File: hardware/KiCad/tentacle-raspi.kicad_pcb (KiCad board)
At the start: 2 copper layers, 65 x 56.5 mm, 37 parts, among them P101 CONN_01X06, P102 CONN_01X06, P201 BNC, P301 BNC, P401 BNC

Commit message: Version 2.0
1wire sensor
flow sensor
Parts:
- removed P102: CONN_01X06, temp_terminal:WL-PINH_1X6_snk
- removed P401: BNC, temp_terminal:WL-EB08040502_snk
- removed STP401: EZO_SMD, temp_terminal:WL-ezo-smd
- added J1: Conn_01x03, Connector_Phoenix_MC:PhoenixContact_MC_1,5_3-G-3.5_1x03_P3.50mm_Horizontal, F.Cu at (153.5, 105.3)
- added J2: Conn_01x03, Connector_Phoenix_MC:PhoenixContact_MC_1,5_3-G-3.5_1x03_P3.50mm_Horizontal, F.Cu at (162.2, 98.0)
- added R1: 4.7K, temp_terminal:WL-SM0805R, F.Cu at (157.7, 95.5)
- added R2: 4.7K, temp_terminal:WL-SM0805R, F.Cu at (156.0, 99.8)
- moved R101 6.25 mm to (162.6, 75.4)
- moved R102 3.97 mm to (162.6, 79.9), turned to -90 degrees
- moved fiducial 1.86 mm to (165.4, 106.2)
- moved fiducial 1.78 mm to (109.2, 65.3)
- moved fiducial 0.57 mm to (107.4, 65.3)
- moved PI_Board 0.55 mm to (138.0, 61.5)
- moved P101 0.21 mm to (167.6, 72.6)
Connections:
- PI_BOARD101 pad 33: unconnected-(PI_BOARD101-Pad33) -> /nonisolated1/TEMP
- PI_BOARD101 pad 37: unconnected-(PI_BOARD101-Pad37) -> /nonisolated1/FLOW
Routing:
- net +3.3V: track 144.6 -> 66.5 mm, vias 3 -> 2
- net /SDA: track 162.9 -> 99.0 mm, vias 5 -> 4
- net /nonisolated1/TEMP: track 0.00 -> 44.0 mm
- net /nonisolated1/FLOW: track 0.00 -> 36.5 mm
- net /SCL: track 135.3 -> 104.6 mm, vias 5 -> 4
- net Net-(R302-Pad2): track 42.9 -> 33.0 mm
- net GND: track 56.5 -> 49.4 mm, vias 13 -> 12
- net Net-(P401-Pad1): track 6.56 -> 0.00 mm
- net Net-(P401-Pad2): track 6.43 -> 0.00 mm
- net Net-(P102-Pad5): track 2.57 -> 0.00 mm
- added copper zone on F.Cu, net +3.3V
- removed copper zone on F.Cu, net GND
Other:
- board text added: "FLOW"
- board text added: "I2C AUX CHANNEL"
- board text added: "TEMP"
- board text removed: "CHANNEL 3"
- board text removed: "CHANNEL 4"
- board text removed: "CHANNEL 5"
- board text removed: "NON ISOLATED"

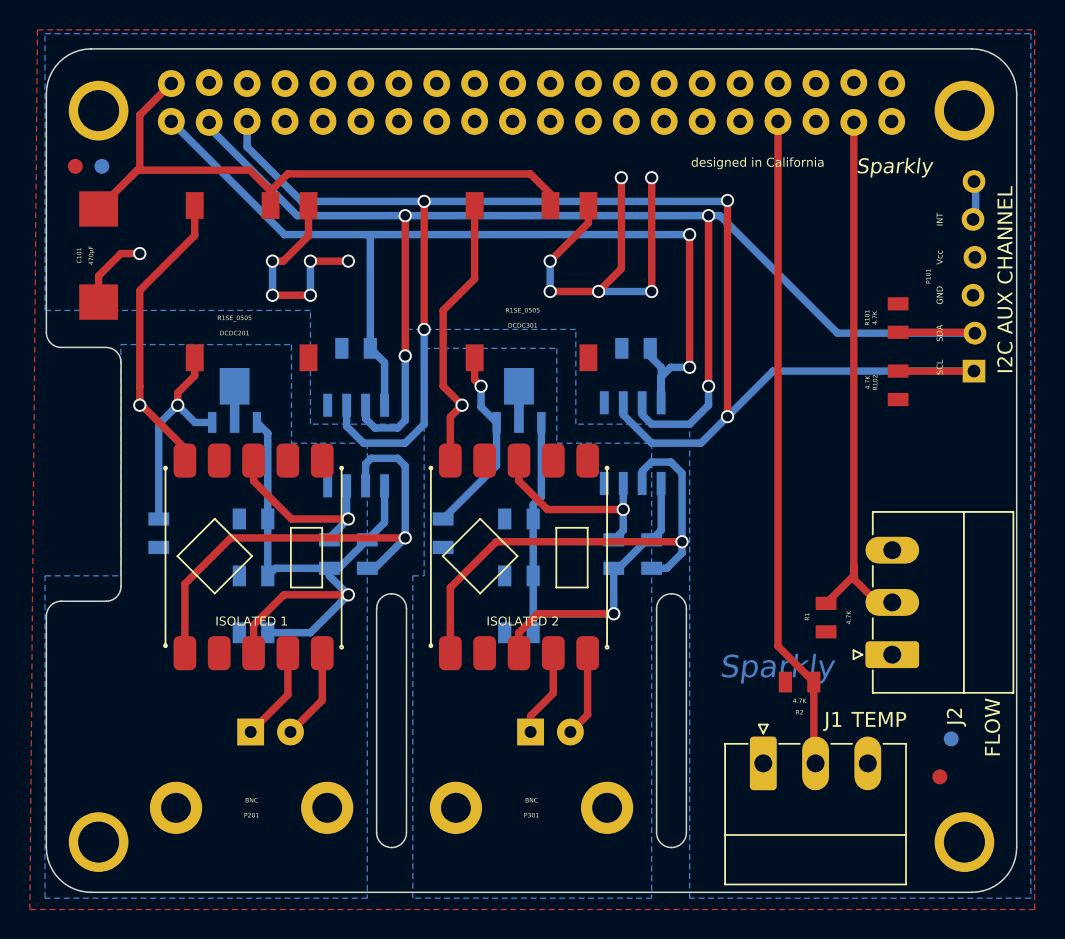
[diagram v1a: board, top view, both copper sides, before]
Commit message: V3, 1wire Temp sensor and flow sensor.
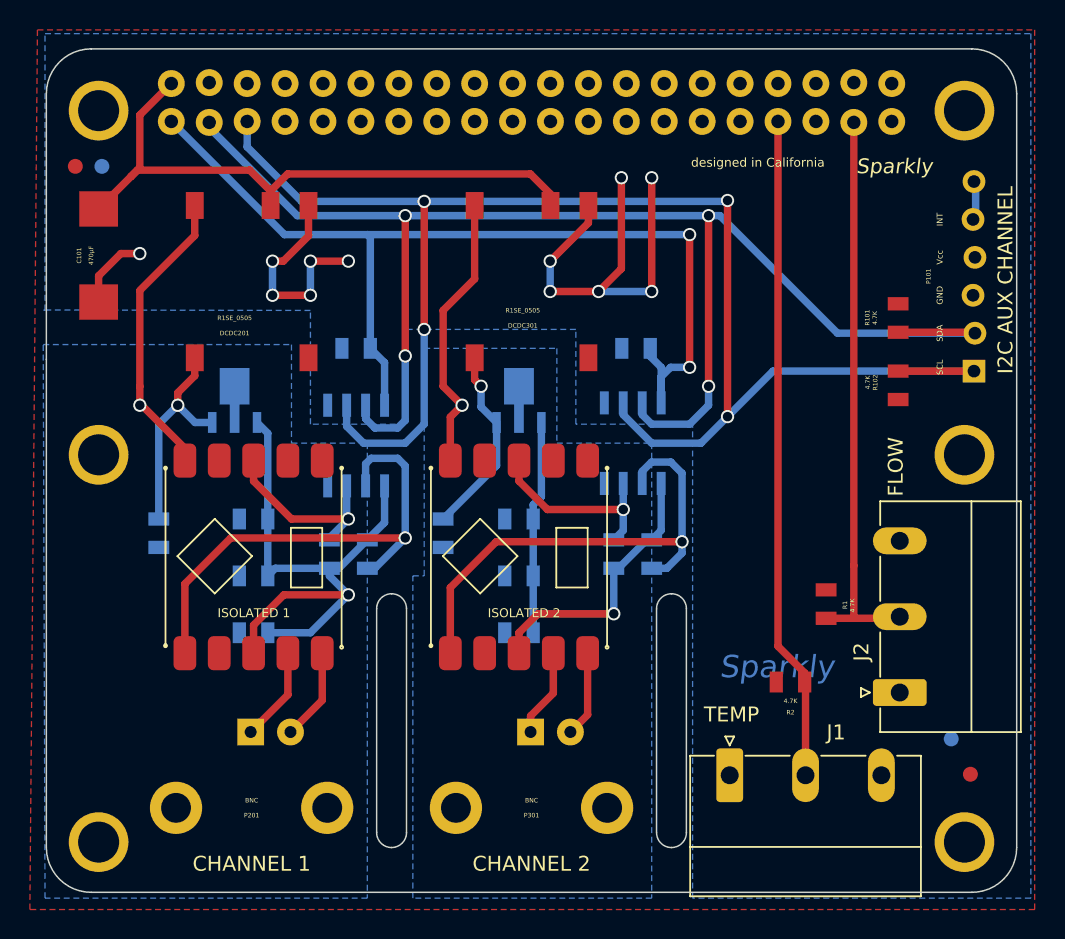
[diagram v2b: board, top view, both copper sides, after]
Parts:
- added ?: , , F.Cu at (167.0, 84.6)
- added ?: , , F.Cu at (109.0, 84.6)
- J1, J2: footprint Connector_Phoenix_MC:PhoenixContact_MC_1,5_3-G-3.5_1x03_P3.50mm_Horizontal -> Connector_Phoenix_MC_HighVoltage:PhoenixContact_MC_1,5_3-G-5.08_1x03_P5.08mm_Horizontal
- moved J2 2.59 mm to (162.7, 100.5)
- moved J1 2.39 mm to (151.3, 106.1)
- moved fiducial 2.05 mm to (167.4, 106.0)
- moved R1 0.90 mm to (157.7, 94.6), turned to 90 degrees
- moved R2 0.61 mm to (155.3, 99.8)
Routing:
- net /nonisolated1/FLOW: track 36.5 -> 37.8 mm
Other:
- outline, holes or cut-outs redrawn
